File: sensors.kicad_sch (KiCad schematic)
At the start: 0 parts

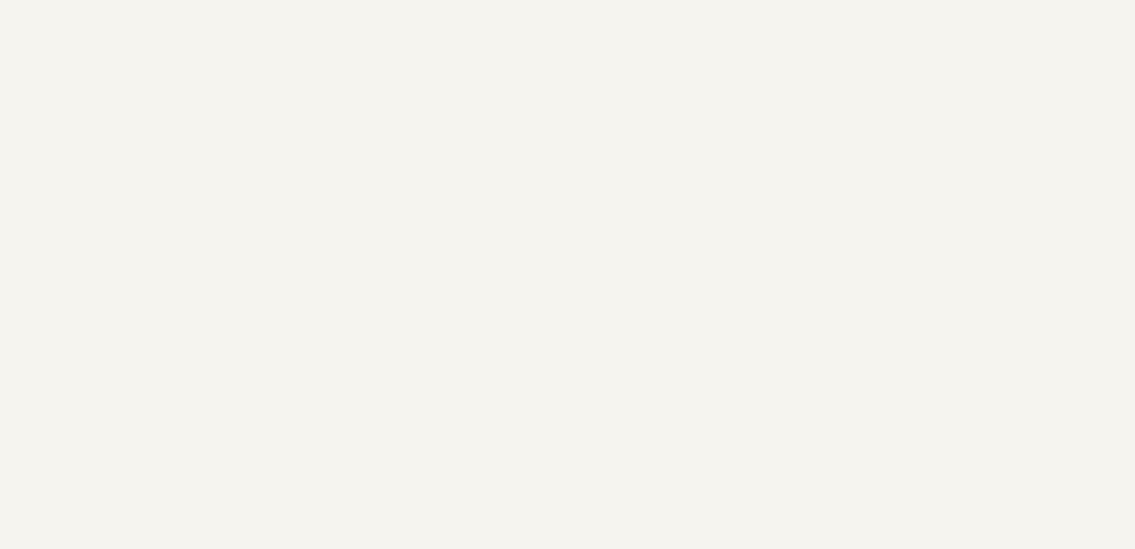
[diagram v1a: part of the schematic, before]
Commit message: update sensors sheet
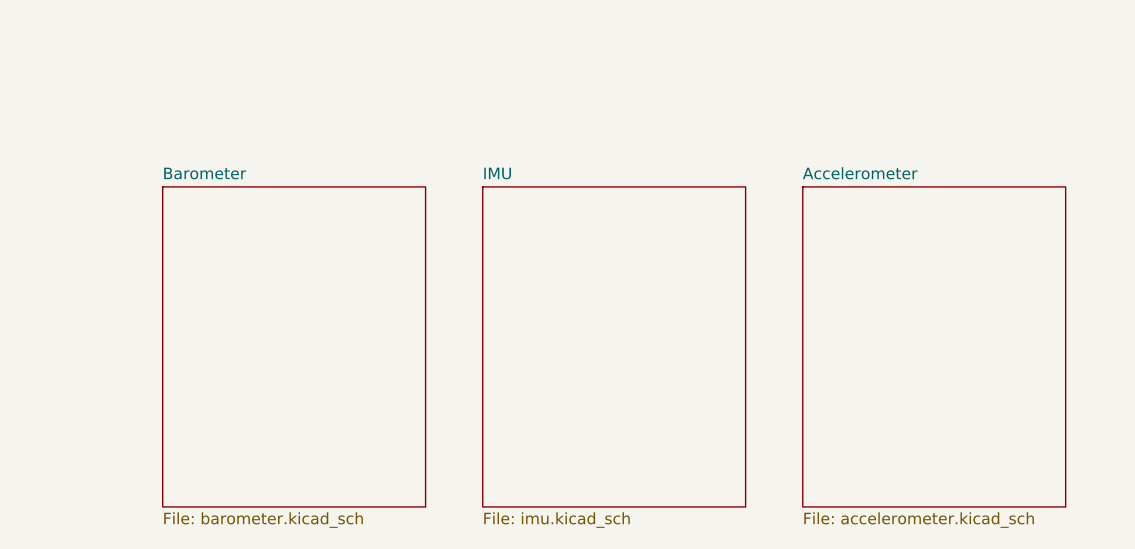
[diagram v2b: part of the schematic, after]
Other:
- added sheet Accelerometer (accelerometer.kicad_sch)
- added sheet Barometer (barometer.kicad_sch)
- added sheet IMU (imu.kicad_sch)
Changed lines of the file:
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@@
+		)
+	)
+	(sheet
+		(at 113.03 63.5)
+		(size 29.21 35.56)
+		(exclude_from_sim no)
+		(in_bom yes)
+		(on_board yes)
+		(dnp no)
+		(fields_autoplaced yes)
+		(stroke
+			(width 0.1524)
+			(type solid)
+		)
+		(fill
+			(color 0 0 0 0.0000)
+		)
+		(property "Sheetname" "IMU"
+			(at 113.03 62.7884 0)
+			(effects
+				(font
+					(size 1.27 1.27)
+				)
+				(justify left bottom)
+			)
+		)
+		(property "Sheetfile" "imu.kicad_sch"
+			(at 113.03 99.6446 0)
+			(effects
+				(font
+					(size 1.27 1.27)
+				)
+				(justify left top)
+			)
+		)
+		(instances
+			(project "Blaze-NT"
+				(path "/2c2eadf0-5503-4531-8753-1a232087fe8c/b9b0c40a-7771-4bc1-adbf-abe0201c34d0"
+					(page "7")
+				)
+			)
+		)
+	)
+	(sheet
+		(at 148.59 63.5)
+		(size 29.21 35.56)
+		(exclude_from_sim no)
+		(in_bom yes)
+		(on_board yes)
+		(dnp no)
+		(fields_autoplaced yes)
+		(stroke
+			(width 0.1524)
+			(type solid)
+		)
+		(fill
+			(color 0 0 0 0.0000)
+		)
+		(property "Sheetname" "Accelerometer"
+			(at 148.59 62.7884 0)
+			(effects
+				(font
+					(size 1.27 1.27)
+				)
+				(justify left bottom)
+			)
+		)
+		(property "Sheetfile" "accelerometer.kicad_sch"
+			(at 148.59 99.6446 0)
+			(effects
+				(font
+					(size 1.27 1.27)
+				)
+				(justify left top)
+			)
+		)
+		(instances
+			(project "Blaze-NT"
+				(path "/2c2eadf0-5503-4531-8753-1a232087fe8c/b9b0c40a-7771-4bc1-adbf-abe0201c34d0"
+					(page "8")
+				)
+			)
+		)
+	)
+	(sheet
+		(at 77.47 63.5)
+		(size 29.21 35.56)
+		(exclude_from_sim no)
+		(in_bom yes)
+		(on_board yes)
+		(dnp no)
+		(fields_autoplaced yes)
+		(stroke
+			(width 0.1524)
+			(type solid)
+		)
+		(fill
+			(color 0 0 0 0.0000)
+		)
+		(property "Sheetname" "Barometer"
+			(at 77.47 62.7884 0)
+			(effects
+				(font
+					(size 1.27 1.27)
+				)
+				(justify left bottom)
+			)
+		)
+		(property "Sheetfile" "barometer.kicad_sch"
+			(at 77.47 99.6446 0)
+			(effects
+				(font
+					(size 1.27 1.27)
+				)
+				(justify left top)
+			)
+		)
+		(instances
+			(project "Blaze-NT"
+				(path "/2c2eadf0-5503-4531-8753-1a232087fe8c/b9b0c40a-7771-4bc1-adbf-abe0201c34d0"
+					(page "7")
+				)
+			)
 		)
 	)
